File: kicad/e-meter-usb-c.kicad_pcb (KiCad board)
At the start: 2 copper layers, 53.8 x 37.6 mm, 39 parts, among them J1 6P6C, J2 USB_C_Receptacle_USB2.0, Q1 S8050, Q3 S8050, Q4 S8050, SW1 SW_Push, U1 AP2112K-3.3, U2 ESP32-WROOM-32, U3 CH340C

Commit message: Change a few components
I could not find the USB converter CH340C so went for CH340B instead.

Same for the 3.3 Volt converter. I had to change it to another one, but
even that one is not available at JLCPCB so I will have to solder it by
hand.
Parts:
- removed R1: 100K, Resistor_SMD:R_0201_0603Metric_Pad0.64x0.40mm_HandSolder
- removed U3: CH340C, Package_SO:SOIC-16_3.9x9.9mm_P1.27mm
- added U4: CH340B (or C), Package_SO:SOIC-16_3.9x9.9mm_P1.27mm, F.Cu at (123.2, 33.3)
- C2: value 10u -> 470p
- C3: value 1u -> 2.2u
- C7: value 100n -> 0.1u
- R11, R3, R7: value 1k -> 60
- U1: value AP2112K-3.3 -> MIC5219-3.3YM5
- moved C1 7.88 mm to (128.5, 46.0), turned to 90 degrees
- moved C2 6.72 mm to (129.5, 52.5), turned to 180 degrees
- moved C3 1.97 mm to (130.7, 45.9)
- moved TP5 0.52 mm to (130.8, 39.6)
- moved TP3 0.46 mm to (123.7, 46.0)
- moved U1 0.39 mm to (129.6, 49.8), turned to 0 degrees
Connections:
- C2 pad 1: +3V3 -> Net-(C2-Pad1)
- U1 pad 3: Net-(R1-Pad1) -> /VCC
- U1 pad 4: Net-(U1-Pad4) -> Net-(C2-Pad1)
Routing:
- net /UART_DTR: track 25.1 -> 28.0 mm
- net +3V3: track 107.3 -> 104.9 mm
- net /VCC: track 32.1 -> 29.9 mm
- net Net-(C2-Pad1): track 0.00 -> 1.91 mm
- net Net-(R1-Pad1): track 1.77 -> 0.00 mm
- net GND: vias 19 -> 20

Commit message: Small updates, first order
This was ordered from JLCPCB late yesterday evening.
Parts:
- R11, R3, R7: value 60 -> 68
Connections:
- net /VCC renamed VCC
- SW1 pad 1: GND -> /ESP_EN
- SW1 pad 2: /ESP_EN -> GND
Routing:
- net GND: track 46.5 -> 42.4 mm, vias 20 -> 18
- net /ESP_EN: track 24.9 -> 28.9 mm, vias 2 -> 4
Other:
- board text added: "Jakob Ruhe"

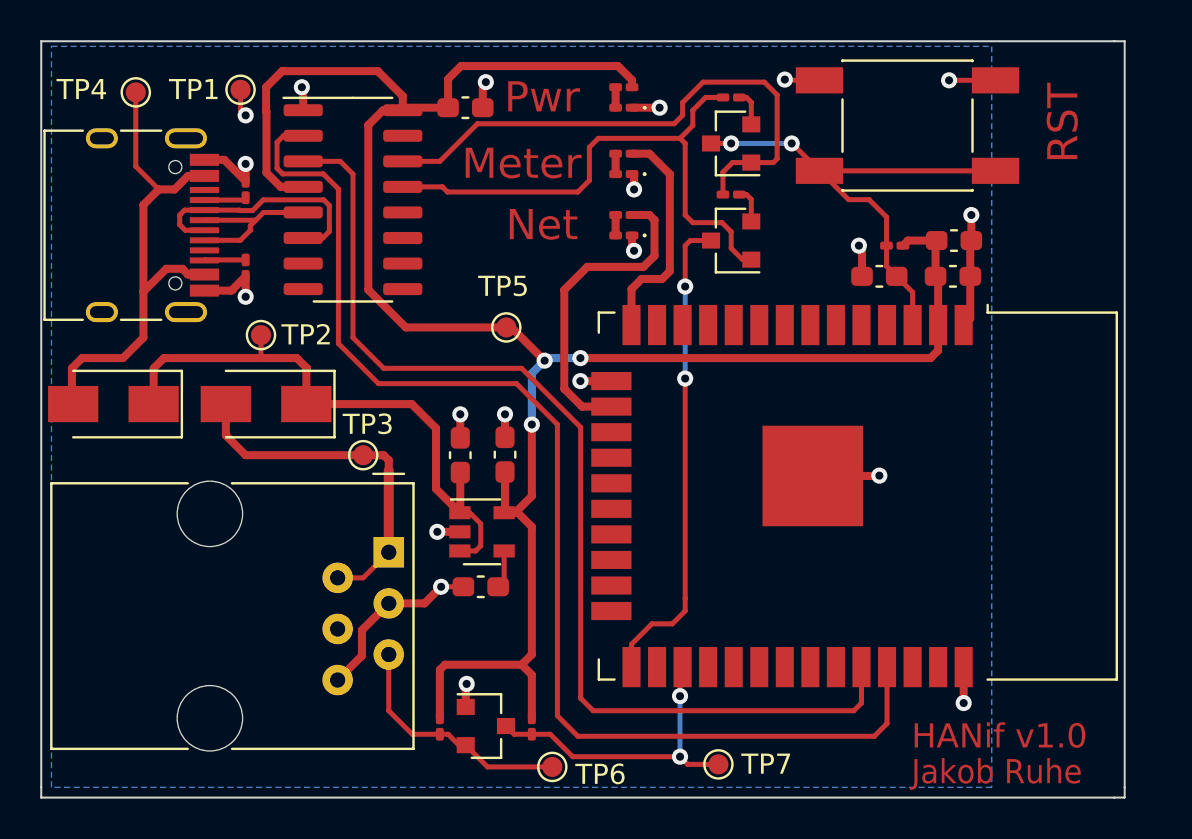
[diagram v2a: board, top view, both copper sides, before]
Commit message: Fix resistors, LEDs and text
I used a too small footprint for resistors and LEDs for the first order.
This fixes that and also puts more text in the silk layer.
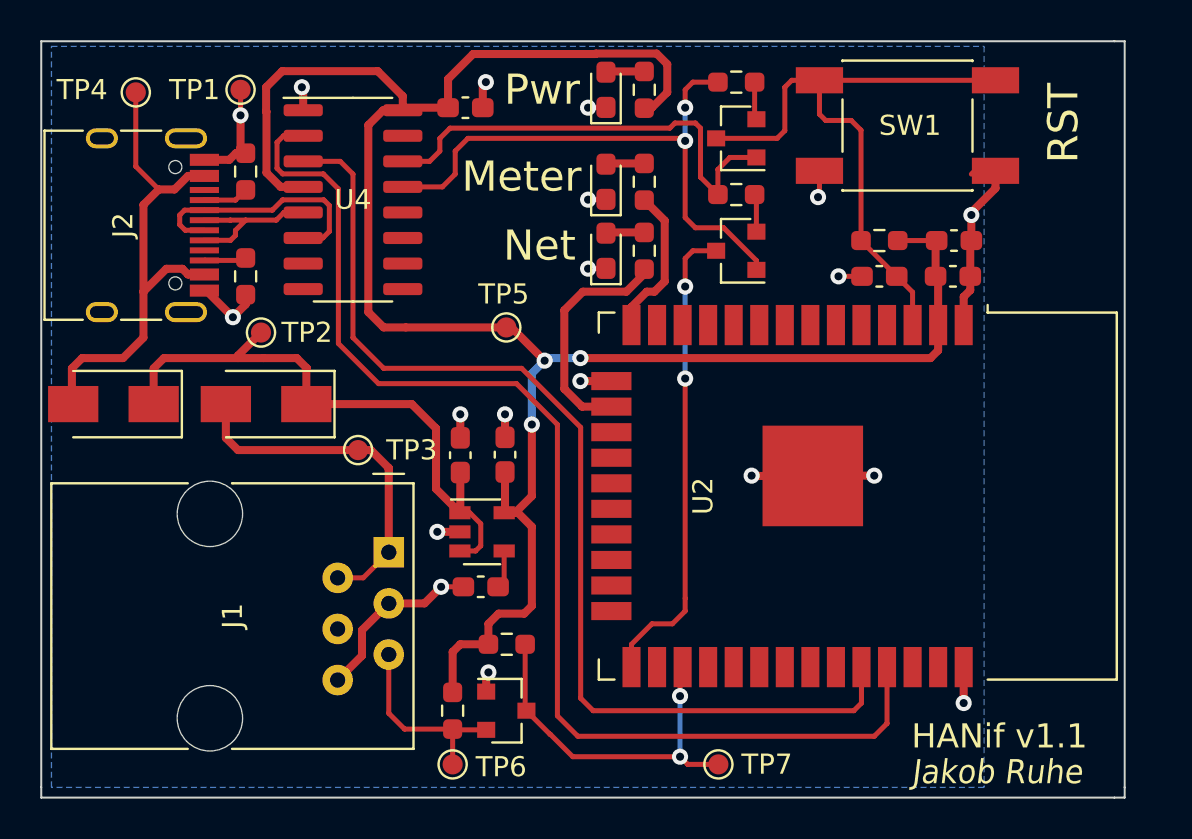
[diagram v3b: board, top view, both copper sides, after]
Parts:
- D3, D4, D5: footprint LED_SMD:LED_0201_0603Metric_Pad0.64x0.40mm_HandSolder -> LED_SMD:LED_0603_1608Metric_Pad1.05x0.95mm_HandSolder
- R10, R11, R2, R3, R4, R5, R6, R7, R8, R9: footprint Resistor_SMD:R_0201_0603Metric_Pad0.64x0.40mm_HandSolder -> Resistor_SMD:R_0603_1608Metric_Pad0.98x0.95mm_HandSolder
- moved TP6 4.95 mm to (128.1, 61.3)
- moved R4 4.25 mm to (130.8, 55.4), turned to 180 degrees
- moved R11 2.05 mm to (137.7, 35.8), turned to 270 degrees
- moved R7 1.73 mm to (137.7, 32.4), turned to 270 degrees
- moved Q1 1.27 mm to (130.8, 58.7)
- moved D3 1.26 mm to (135.8, 27.8), turned to 90 degrees
- moved D5 1.17 mm to (135.8, 35.8), turned to 90 degrees
- moved R3 1.02 mm to (137.7, 27.8), turned to 270 degrees
- moved R2 0.99 mm to (128.1, 58.7)
- moved D4 0.97 mm to (135.8, 32.4), turned to 90 degrees
- moved R8 0.89 mm to (117.9, 31.9)
- moved R5 0.80 mm to (142.2, 27.4)
- moved R10 0.80 mm to (149.4, 35.3)
- moved Q4 0.57 mm to (142.2, 35.8)
- moved R9 0.41 mm to (117.9, 37.1)
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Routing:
- net GND: track 42.4 -> 48.9 mm, vias 18 -> 19
- net /UART_RTS: track 28.1 -> 23.4 mm
- net /NETWORK_LED: track 15.8 -> 11.6 mm
- net /METER_LED: track 11.2 -> 7.54 mm
- net /HAN_TO_ESP: track 15.9 -> 18.5 mm
- net /ESP_EN: track 28.9 -> 31.2 mm, vias 4 -> 0
- net /HAN_DATA: track 12.1 -> 9.86 mm
- net Net-(D5-Pad2): track 1.02 -> 1.92 mm
- net Net-(D4-Pad2): track 1.02 -> 1.92 mm
- net Net-(D3-Pad2): track 1.02 -> 1.92 mm
- net VCC: track 29.9 -> 30.5 mm
- net /UART_DTR: track 28.0 -> 28.5 mm, vias 0 -> 2
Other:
- board text added: "HANif v1.1"
- board text removed: "HANif v1.0"
